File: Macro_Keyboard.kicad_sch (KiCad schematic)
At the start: 21 parts, among them SW1 SW_Push, SW2 SW_Push, U1 STM32L432KCUx, U2 LD39050PU33R

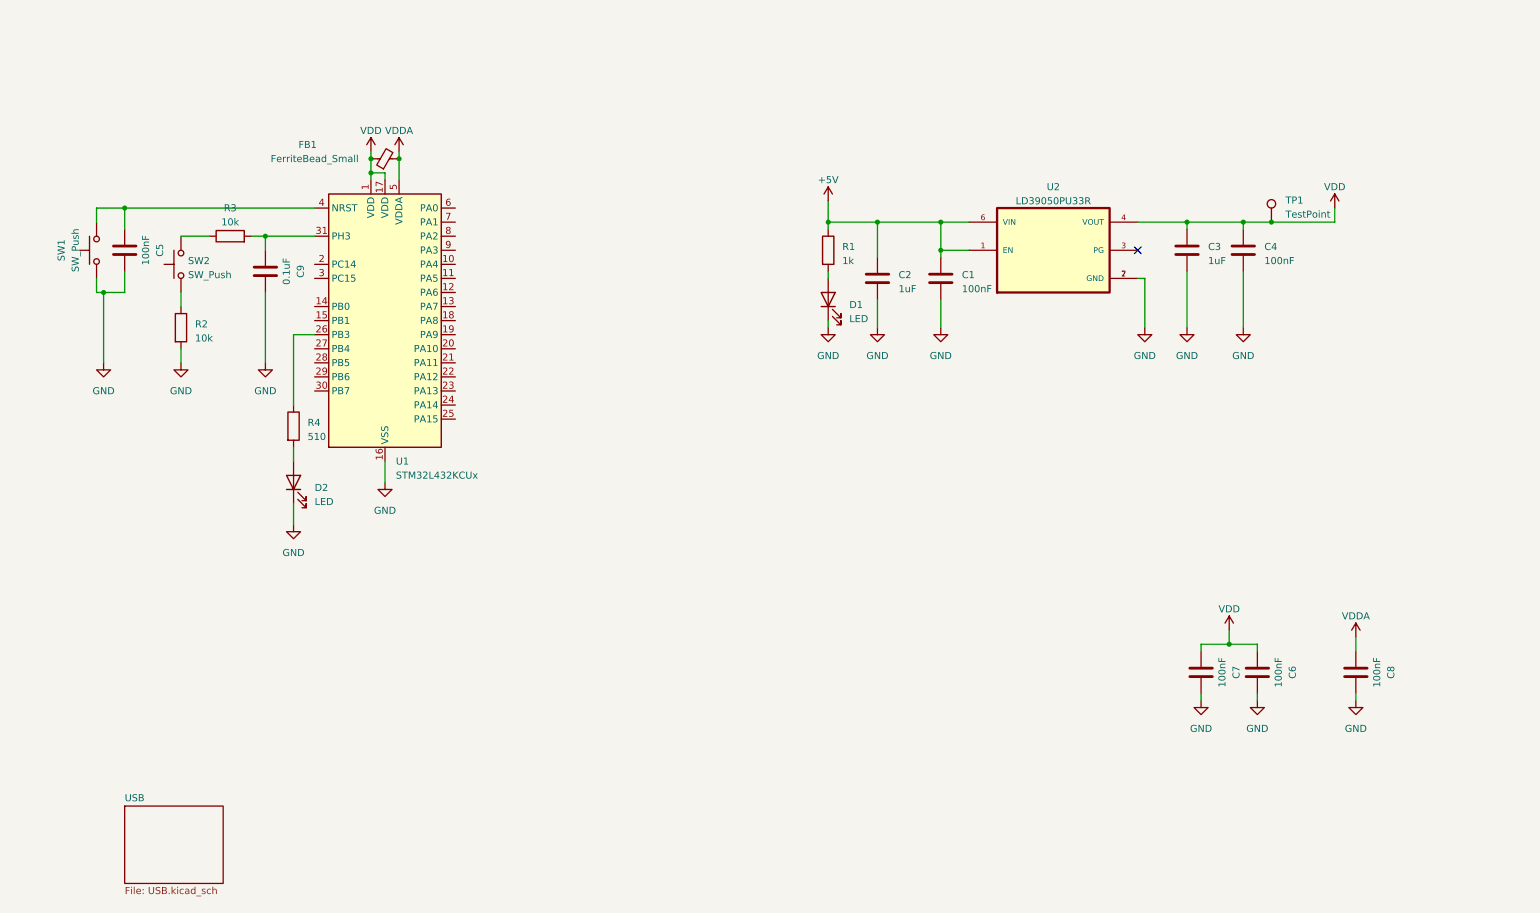
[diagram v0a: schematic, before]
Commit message: Schematic fertig und Layout gerouted
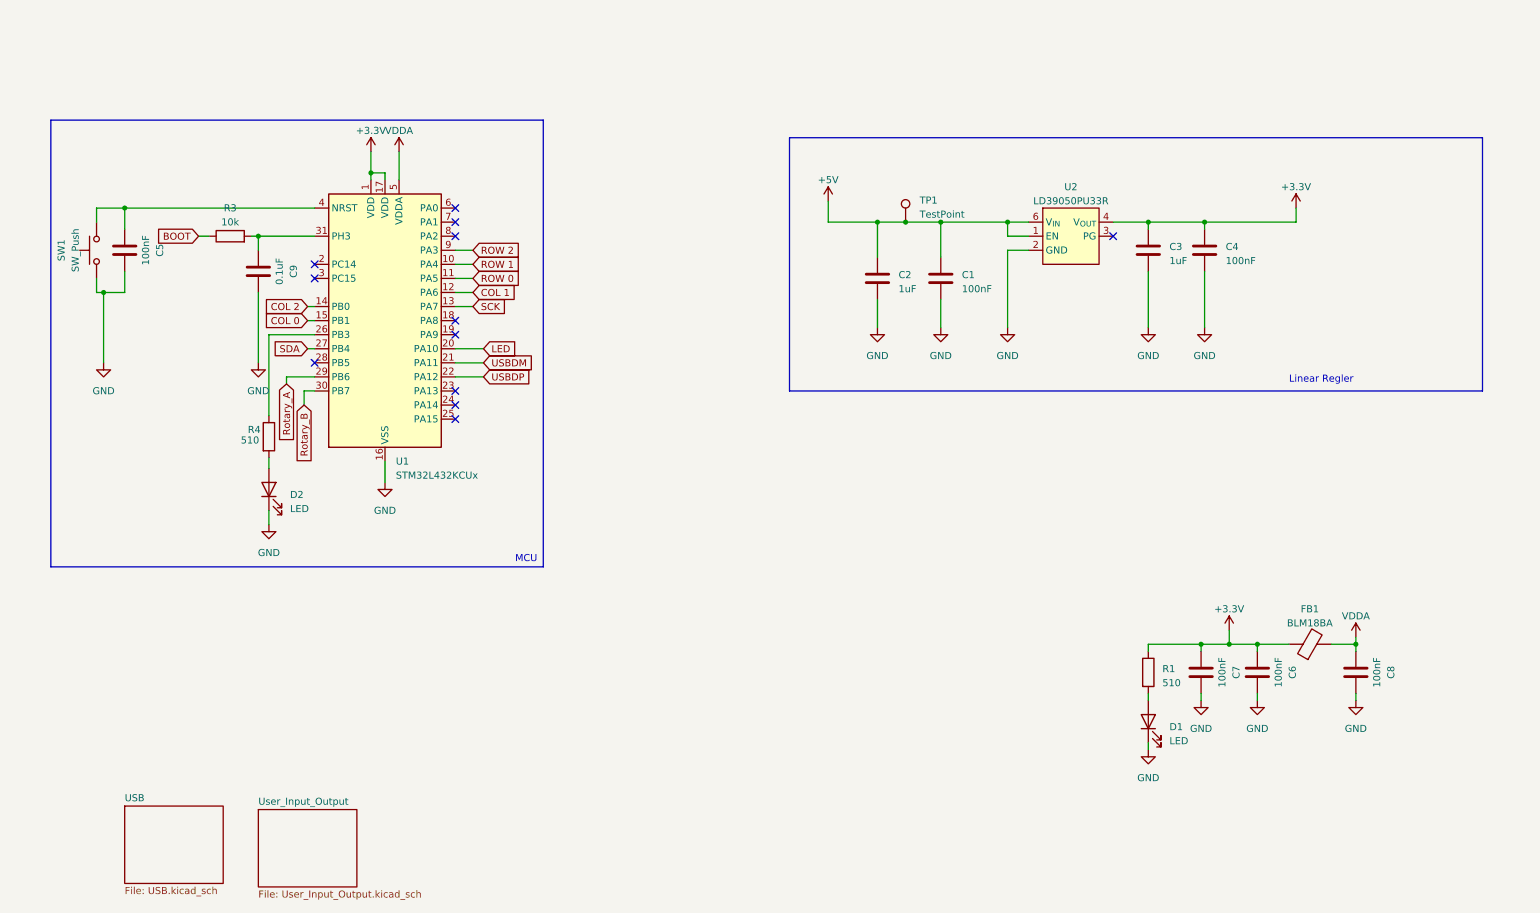
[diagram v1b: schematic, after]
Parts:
- removed FB1: FerriteBead_Small, symbol Device:FerriteBead_Small
- removed R2: 10k, symbol Device:R
- removed SW2: SW_Push, symbol Switch:SW_Push
- removed U2: LD39050PU33R, SON95P300X300X100-7N, symbol LD39050PU33R:LD39050PU33R
- added FB1: BLM18BA, Inductor_SMD:L_0603_1608Metric_Pad1.05x0.95mm_HandSolder, symbol Device:FerriteBead
- added U2: LD39050PU33R, custom:LD39050_DFN6, symbol custom:LD39050PU33R
- C1: footprint (none) -> Inductor_SMD:L_0603_1608Metric_Pad1.05x0.95mm_HandSolder
- C2, C3: footprint (none) -> Capacitor_SMD:CP_Elec_4x5.4
- C4, C5, C6, C7, C8, C9: footprint (none) -> Capacitor_SMD:C_0805_2012Metric_Pad1.18x1.45mm_HandSolder
- D1, D2: footprint (none) -> LED_SMD:LED_0805_2012Metric_Pad1.15x1.40mm_HandSolder
- R1: value 1k -> 510; footprint (none) -> Resistor_SMD:R_1206_3216Metric_Pad1.30x1.75mm_HandSolder
- R3, R4: footprint (none) -> Resistor_SMD:R_1206_3216Metric_Pad1.30x1.75mm_HandSolder
- SW1: footprint (none) -> Button_Switch_THT:SW_Tactile_SPST_Angled_PTS645Vx31-2LFS
- TP1: footprint (none) -> Connector_PinHeader_2.54mm:PinHeader_1x01_P2.54mm_Vertical
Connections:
- net +5V: now also TP1.1, U2.1 (EN), U2.6 (V_{IN}); no longer R1.1
- net GND: now also U2.2 (GND), U2.5 (GND)
- net VDDA: now also FB1.2
- net ROW 1: now reaches U1.10 (PA4)
- net ROW 0: now reaches U1.11 (PA5)
- net COL 1: now reaches U1.12 (PA6)
- net SCK: now reaches U1.13 (PA7)
- net COL 2: now reaches U1.14 (PB0)
- net COL 0: now reaches U1.15 (PB1)
- net LED: now reaches U1.20 (PA10)
- net USBDM: now reaches U1.21 (PA11)
- net USBDP: now reaches U1.22 (PA12)
- net SDA: now reaches U1.27 (PB4)
- net Rotary_A: now reaches U1.29 (PB6)
- net Rotary_B: now reaches U1.30 (PB7)
- net ROW 2: now reaches U1.9 (PA3)
- net BOOT: now reaches R3.1
- net VDD renamed +3.3V
- net +3.3V: now also R1.1, FB1.1, U2.4 (V_{OUT}); no longer TP1.1
- no-connect marks 1 -> 12
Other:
- added sheet User_Input_Output (User_Input_Output.kicad_sch)
- note added: "Linear Regler"
- note added: "MCU"
- moved on the sheet: C3, C4, C9, D2, R4, TP1

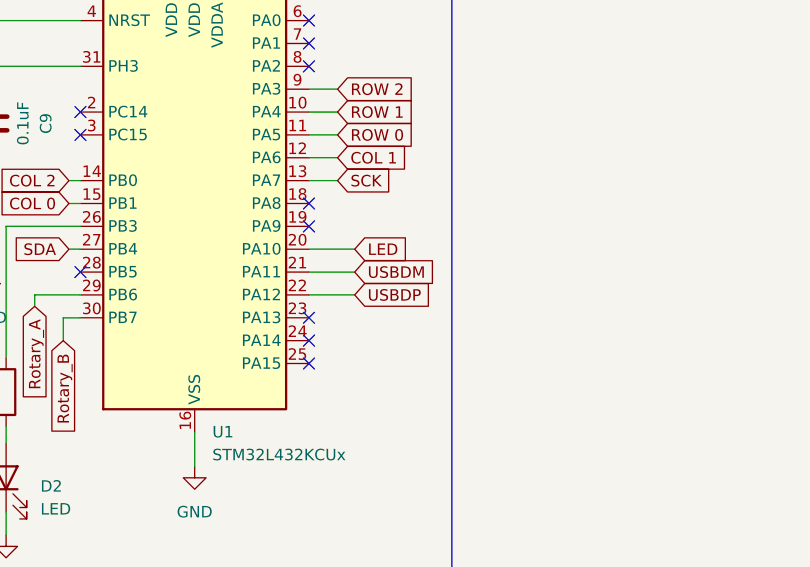
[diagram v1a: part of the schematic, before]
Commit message: Neue Anordnung für bessere Usb Leitungen
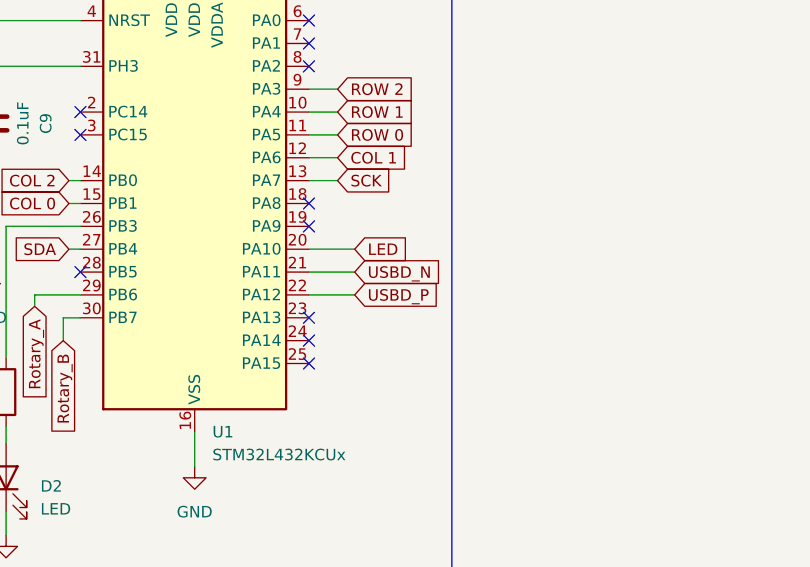
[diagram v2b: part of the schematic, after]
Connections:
- net USBDM renamed USBD_N
- net USBDP renamed USBD_P
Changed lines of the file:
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@@
     )
   )
-  (global_label "USBDP" (shape input) (at 97.79 78.74 0) (fields_autoplaced)
+  (global_label "USBD_P" (shape input) (at 97.79 78.74 0) (fields_autoplaced)
     (effects (font (size 1.27 1.27)) (justify left))
-    (property "Intersheetrefs" "${INTERSHEET_REFS}" (at 107.0458 78.74 0)
+    (property "Intersheetrefs" "${INTERSHEET_REFS}" (at 108.0134 78.74 0)
       (effects (font (size 1.27 1.27)) (justify left) hide)
     )
@@
     )
   )
-  (global_label "USBDM" (shape input) (at 97.79 76.2 0) (fields_autoplaced)
+  (global_label "USBD_N" (shape input) (at 97.79 76.2 0) (fields_autoplaced)
     (effects (font (size 1.27 1.27)) (justify left))
-    (property "Intersheetrefs" "${INTERSHEET_REFS}" (at 107.2272 76.2 0)
+    (property "Intersheetrefs" "${INTERSHEET_REFS}" (at 108.0739 76.2 0)
       (effects (font (size 1.27 1.27)) (justify left) hide)
     )

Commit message: Add files via upload
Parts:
- added C17: 10uF, Capacitor_SMD:CP_Elec_4x5.8, symbol Device:C_Polarized_US
- C2, C3: footprint Capacitor_SMD:CP_Elec_4x5.4 -> Capacitor_SMD:C_0603_1608Metric_Pad1.08x0.95mm_HandSolder
- C4, C5, C6, C7, C8, C9: footprint Capacitor_SMD:C_0805_2012Metric_Pad1.18x1.45mm_HandSolder -> Capacitor_SMD:C_0603_1608Metric_Pad1.08x0.95mm_HandSolder
- R1, R3, R4: footprint Resistor_SMD:R_1206_3216Metric_Pad1.30x1.75mm_HandSolder -> Resistor_SMD:R_0805_2012Metric_Pad1.20x1.40mm_HandSolder
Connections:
- net +3.3V: now also C17.1
- net GND: now also C17.2
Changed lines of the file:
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@@
   (junction (at 227.965 50.8) (diameter 0) (color 0 0 0 0)
+  )
+  (junction (at 240.03 50.8) (diameter 0) (color 0 0 0 0)
   )
   (junction (at 168.91 50.8) (diameter 0) (color 0 0 0 0)
@@
     (stroke (width 0) (type default))
   )
-  (wire (pts (xy 227.965 50.8) (xy 244.475 50.8))
+  (wire (pts (xy 227.965 50.8) (xy 240.03 50.8))
     (stroke (width 0) (type default))
   )
@@
     (stroke (width 0) (type default))
   )
+  (wire (pts (xy 240.03 50.8) (xy 244.475 50.8))
+    (stroke (width 0) (type default))
+  )
   (wire (pts (xy 92.71 55.88) (xy 95.885 55.88))
     (stroke (width 0) (type default))
@@
   )
   (wire (pts (xy 255.27 135.89) (xy 255.27 137.16))
+    (stroke (width 0) (type default))
+  )
+  (wire (pts (xy 240.03 59.69) (xy 240.03 69.85))
+    (stroke (width 0) (type default))
+  )
+  (wire (pts (xy 240.03 50.8) (xy 240.03 52.07))
     (stroke (width 0) (type default))
   )
@@
       (effects (font (size 1.27 1.27)))
     )
-    (property "Footprint" "Capacitor_SMD:C_0805_2012Metric_Pad1.18x1.45mm_HandSolder" (at 238.4552 135.89 0)
+    (property "Footprint" "Capacitor_SMD:C_0603_1608Metric_Pad1.08x0.95mm_HandSolder" (at 238.4552 135.89 0)
       (effects (font (size 1.27 1.27)) hide)
     )
@@
         (path "/41b3a189-fb3d-44ed-903d-e385e89f379a"
           (reference "#PWR07") (unit 1)
+        )
+      )
+    )
+  )
+  (symbol (lib_id "Device:C_Polarized_US") (at 240.03 55.88 0) (unit 1)
+    (in_bom yes) (on_board yes) (dnp no) (fields_autoplaced)
+    (property "Reference" "C17" (at 243.84 54.61 0)
+      (effects (font (size 1.27 1.27)) (justify left))
+    )
+    (property "Value" "10uF" (at 243.84 57.15 0)
+      (effects (font (size 1.27 1.27)) (justify left))
+    )
+    (property "Footprint" "Capacitor_SMD:CP_Elec_4x5.8" (at 240.03 55.88 0)
+      (effects (font (size 1.27 1.27)) hide)
+    )
+    (property "Datasheet" "~" (at 240.03 55.88 0)
+      (effects (font (size 1.27 1.27)) hide)
+    )
+    (pin "1")
+    (pin "2")
+    (instances
+      (project "Macro_Keyboard"
+        (path "/41b3a189-fb3d-44ed-903d-e385e89f379a/7616f98b-14aa-434e-b39a-d33e4927fb29"
+          (reference "C17") (unit 1)
+        )
+        (path "/41b3a189-fb3d-44ed-903d-e385e89f379a"
+          (reference "C14") (unit 1)
         )
       )
@@
       (effects (font (size 1.27 1.27)))
     )
-    (property "Footprint" "Capacitor_SMD:C_0805_2012Metric_Pad1.18x1.45mm_HandSolder" (at 256.2352 135.89 0)
+    (property "Footprint" "Capacitor_SMD:C_0603_1608Metric_Pad1.08x0.95mm_HandSolder" (at 256.2352 135.89 0)
       (effects (font (size 1.27 1.27)) hide)
     )
@@
       (effects (font (size 1.27 1.27)) (justify left))
     )
-    (property "Footprint" "Resistor_SMD:R_1206_3216Metric_Pad1.30x1.75mm_HandSolder" (at 216.027 132.08 90)
+    (property "Footprint" "Resistor_SMD:R_0805_2012Metric_Pad1.20x1.40mm_HandSolder" (at 216.027 132.08 90)
       (effects (font (size 1.27 1.27)) hide)
     )
@@
       (effects (font (size 1.27 1.27)) (justify left))
     )
-    (property "Footprint" "Capacitor_SMD:CP_Elec_4x5.4" (at 218.7702 59.69 0)
+    (property "Footprint" "Capacitor_SMD:C_0603_1608Metric_Pad1.08x0.95mm_HandSolder" (at 218.7702 59.69 0)
       (effects (font (size 1.27 1.27)) hide)
     )
@@
       (effects (font (size 1.27 1.27)) (justify left))
     )
-    (property "Footprint" "Capacitor_SMD:C_0805_2012Metric_Pad1.18x1.45mm_HandSolder" (at 228.9302 59.69 0)
+    (property "Footprint" "Capacitor_SMD:C_0603_1608Metric_Pad1.08x0.95mm_HandSolder" (at 228.9302 59.69 0)
       (effects (font (size 1.27 1.27)) hide)
     )
@@
       (effects (font (size 1.27 1.27)))
     )
-    (property "Footprint" "Resistor_SMD:R_1206_3216Metric_Pad1.30x1.75mm_HandSolder" (at 52.07 55.118 90)
+    (property "Footprint" "Resistor_SMD:R_0805_2012Metric_Pad1.20x1.40mm_HandSolder" (at 52.07 55.118 90)
       (effects (font (size 1.27 1.27)) hide)
     )
@@
       (effects (font (size 1.27 1.27)))
     )
-    (property "Footprint" "Capacitor_SMD:C_0805_2012Metric_Pad1.18x1.45mm_HandSolder" (at 58.1152 63.5 0)
+    (property "Footprint" "Capacitor_SMD:C_0603_1608Metric_Pad1.08x0.95mm_HandSolder" (at 58.1152 63.5 0)
       (effects (font (size 1.27 1.27)) hide)
     )
@@
       (effects (font (size 1.27 1.27)) (justify left))
     )
-    (property "Footprint" "Resistor_SMD:R_1206_3216Metric_Pad1.30x1.75mm_HandSolder" (at 57.277 89.535 90)
+    (property "Footprint" "Resistor_SMD:R_0805_2012Metric_Pad1.20x1.40mm_HandSolder" (at 57.277 89.535 90)
       (effects (font (size 1.27 1.27)) hide)
     )
@@
       (effects (font (size 1.27 1.27)))
     )
-    (property "Footprint" "Capacitor_SMD:C_0805_2012Metric_Pad1.18x1.45mm_HandSolder" (at 33.9852 59.69 0)
+    (property "Footprint" "Capacitor_SMD:C_0603_1608Metric_Pad1.08x0.95mm_HandSolder" (at 33.9852 59.69 0)
       (effects (font (size 1.27 1.27)) hide)
     )
@@
       (effects (font (size 1.27 1.27)))
     )
-    (property "Footprint" "Capacitor_SMD:C_0805_2012Metric_Pad1.18x1.45mm_HandSolder" (at 228.2952 135.89 0)
+    (property "Footprint" "Capacitor_SMD:C_0603_1608Metric_Pad1.08x0.95mm_HandSolder" (at 228.2952 135.89 0)
       (effects (font (size 1.27 1.27)) hide)
     )
@@
         (path "/41b3a189-fb3d-44ed-903d-e385e89f379a"
           (reference "C7") (unit 1)
+        )
+      )
+    )
+  )
+  (symbol (lib_id "power:GND") (at 240.03 69.85 0) (unit 1)
+    (in_bom yes) (on_board yes) (dnp no) (fields_autoplaced)
+    (property "Reference" "#PWR023" (at 240.03 76.2 0)
+      (effects (font (size 1.27 1.27)) hide)
+    )
+    (property "Value" "GND" (at 240.03 74.93 0)
+      (effects (font (size 1.27 1.27)))
+    )
+    (property "Footprint" "" (at 240.03 69.85 0)
+      (effects (font (size 1.27 1.27)) hide)
+    )
+    (property "Datasheet" "" (at 240.03 69.85 0)
+      (effects (font (size 1.27 1.27)) hide)
+    )
+    (pin "1")
+    (instances
+      (project "Macro_Keyboard"
+        (path "/41b3a189-fb3d-44ed-903d-e385e89f379a"
+          (reference "#PWR023") (unit 1)
         )
       )
@@
       (effects (font (size 1.27 1.27)) (justify left))
     )
-    (property "Footprint" "Capacitor_SMD:CP_Elec_4x5.4" (at 169.8752 64.77 0)
-      (effects (font (size 1.27 1.27)) hide)
-    )
+    (property "Footprint" "Capacitor_SMD:C_0603_1608Metric_Pad1.08x0.95mm_HandSolder" (at 169.8752 64.77 0)
+      (effects (font (size 1.27 1.27)) hide)
+    )

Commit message: Add files via upload
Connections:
- net COL 0: now also U1.14 (PB0); no longer U1.15 (PB1)
- net COL 2: now also U1.15 (PB1); no longer U1.14 (PB0)
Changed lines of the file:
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@@
     )
   )
-  (global_label "COL 0" (shape input) (at 66.04 68.58 180) (fields_autoplaced)
+  (global_label "COL 0" (shape input) (at 66.04 66.04 180) (fields_autoplaced)
     (effects (font (size 1.27 1.27)) (justify right))
-    (property "Intersheetrefs" "${INTERSHEET_REFS}" (at 57.5341 68.58 0)
+    (property "Intersheetrefs" "${INTERSHEET_REFS}" (at 57.5341 66.04 0)
       (effects (font (size 1.27 1.27)) (justify right) hide)
     )
@@
     )
   )
-  (global_label "COL 2" (shape input) (at 66.04 66.04 180) (fields_autoplaced)
+  (global_label "COL 2" (shape input) (at 66.04 68.58 180) (fields_autoplaced)
     (effects (font (size 1.27 1.27)) (justify right))
-    (property "Intersheetrefs" "${INTERSHEET_REFS}" (at 57.5341 66.04 0)
+    (property "Intersheetrefs" "${INTERSHEET_REFS}" (at 57.5341 68.58 0)
       (effects (font (size 1.27 1.27)) (justify right) hide)
     )

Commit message: Add files via upload
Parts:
- C1: footprint Inductor_SMD:L_0603_1608Metric_Pad1.05x0.95mm_HandSolder -> (none)
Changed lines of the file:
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@@
       (effects (font (size 1.27 1.27)) (justify left))
     )
-    (property "Footprint" "Inductor_SMD:L_0603_1608Metric_Pad1.05x0.95mm_HandSolder" (at 181.3052 64.77 0)
+    (property "Footprint" "" (at 181.3052 64.77 0)
       (effects (font (size 1.27 1.27)) hide)
     )
